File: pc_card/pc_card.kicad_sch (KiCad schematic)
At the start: 44 parts, among them IC1 SV 3.3V, IC2 74LVC1G00, IC3 SV 4.5V, IC4 TPA152DR, J1 PCMCIA Connector, J2 Headphones Out, U1 Z8601720ASG, U2 25LCxxx, U3 YMF289B-S, U4 YAC516-E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

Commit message: fixes
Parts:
- removed D1: D_Small_ALT, Diode_SMD:D_SOD-323_HandSoldering, symbol pc_card_sound_barker-rescue:D_Small_ALT-Device
- removed IC2: 74LVC1G00, Package_TO_SOT_SMD:SOT-23-5_HandSoldering, symbol pc_card_sound_barker-rescue:74LVC1G00-74xGxx
- removed JP3: Write Protect, Jumper:SolderJumper-3_P1.3mm_Bridged12_RoundedPad1.0x1.5mm_NumberLabels, symbol pc_card_sound_barker-rescue:SolderJumper_3_Bridged12-Jumper
- removed RN1: 20k, Resistor_SMD:R_Array_Convex_4x1206, symbol Device:R_Pack04_Split
- removed U2: 25LCxxx, Package_SO:SOIC-8_3.9x4.9mm_P1.27mm, symbol Memory_EEPROM:25LCxxx
- added R12: EEPROM, Resistor_SMD:R_0603_1608Metric_Pad0.98x0.95mm_HandSolder, symbol Device:R_Small
- added R3, R5, R6, R7: 20k, Resistor_SMD:R_0805_2012Metric_Pad1.20x1.40mm_HandSolder, symbol Device:R
- added U2: 93AAxxC, Package_SO:SOIC-8_3.9x4.9mm_P1.27mm, symbol Memory_EEPROM:93AAxxC
- IC4: footprint SOIC127P600X175-8N -> Package_SO:SOIC-8_3.9x4.9mm_P1.27mm
- U1: footprint QFP50P1600X1600X160-100N -> Package_QFP:LQFP-100_14x14mm_P0.5mm
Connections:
- net EE_CS: now also U2.1 (CS)
- net EE_DI: now also U2.4 (DO)
- net EE_DO: now also U2.3 (DI)
- net EE_SK: now also U2.2 (SCLK)
- net VCC: now also R12.1
- net VPP: now also R12.2, U2.8 (VCC)
- net at C13.1: now also R7.2
- net at IC4.8 (IN1-): now also R6.2, R7.1
- net at C10.2, IC4.1 (VO1), R4.2: now also R6.1
- net at IC4.4 (IN2-): now also R3.1, R5.2
- net at C14.2, IC4.5 (VO2), R8.1: now also R3.2
- net at C11.1: now also R5.1
- net GND renamed GNDA
- net GNDA: now also U2.5 (GND)
- no-connect marks 44 -> 45

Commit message: devboard; finishing 4L card
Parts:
- removed U2: 93AAxxC, Package_SO:SOIC-8_3.9x4.9mm_P1.27mm, symbol Memory_EEPROM:93AAxxC
- added R13: ORG, Resistor_SMD:R_0603_1608Metric_Pad0.98x0.95mm_HandSolder, symbol Device:R_Small
- added TP3: CS, TestPoint:TestPoint_Keystone_5015_Micro-Minature, symbol Connector:TestPoint_Probe
- added TP4: GND, TestPoint:TestPoint_Pad_D1.0mm, symbol Connector:TestPoint
- added TP5: RESET, TestPoint:TestPoint_Keystone_5015_Micro-Minature, symbol Connector:TestPoint_Probe
- added TP6: PWDN, TestPoint:TestPoint_Keystone_5015_Micro-Minature, symbol Connector:TestPoint_Probe
- added TP7: AUDIO, TestPoint:TestPoint_Keystone_5015_Micro-Minature, symbol Connector:TestPoint_Probe
- added TP8: 5V/~{3V}, TestPoint:TestPoint_Keystone_5015_Micro-Minature, symbol Connector:TestPoint_Probe
- added U2: 93CxxC, Package_SO:SOIC-8_3.9x4.9mm_P1.27mm, symbol Memory_EEPROM:93CxxC
- R10: footprint Resistor_SMD:R_0402_1005Metric_Pad0.72x0.64mm_HandSolder -> Resistor_SMD:R_0603_1608Metric_Pad0.98x0.95mm_HandSolder
- R11: footprint Resistor_SMD:R_1206_3216Metric_Pad1.30x1.75mm_HandSolder -> Resistor_SMD:R_0603_1608Metric_Pad0.98x0.95mm_HandSolder
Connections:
- net EE_CS: now also U2.1 (CS)
- net EE_DI: now also U2.4 (DO)
- net EE_DO: now also U2.3 (DI)
- net EE_SK: now also U2.2 (SCLK)
- net GNDA: now also R13.1, TP4.1, U2.5 (GND), U2.7 (TEST)
- net ICS0#: now also TP3.1
- net POR#: now also TP5.1
- net VPP: now also U2.8 (VCC)
- net at U1.59 (EXTP_PWDN): now also TP6.1
- net at U1.60 (EXTP_AUDIO): now also TP7.1
- net YMFVS renamed 5V/~{3V}
- net 5V/~{3V}: now also TP8.1
- new net: R13.2, U2.6 (ORG)
- no-connect marks 45 -> 42
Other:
- note removed: "Card Barker OPL3 Sound Card"
- note removed: "Nov 30 2021"
- note removed: "Prototype One"
- title: (none) -> Card Barker OPL3 Sound Card

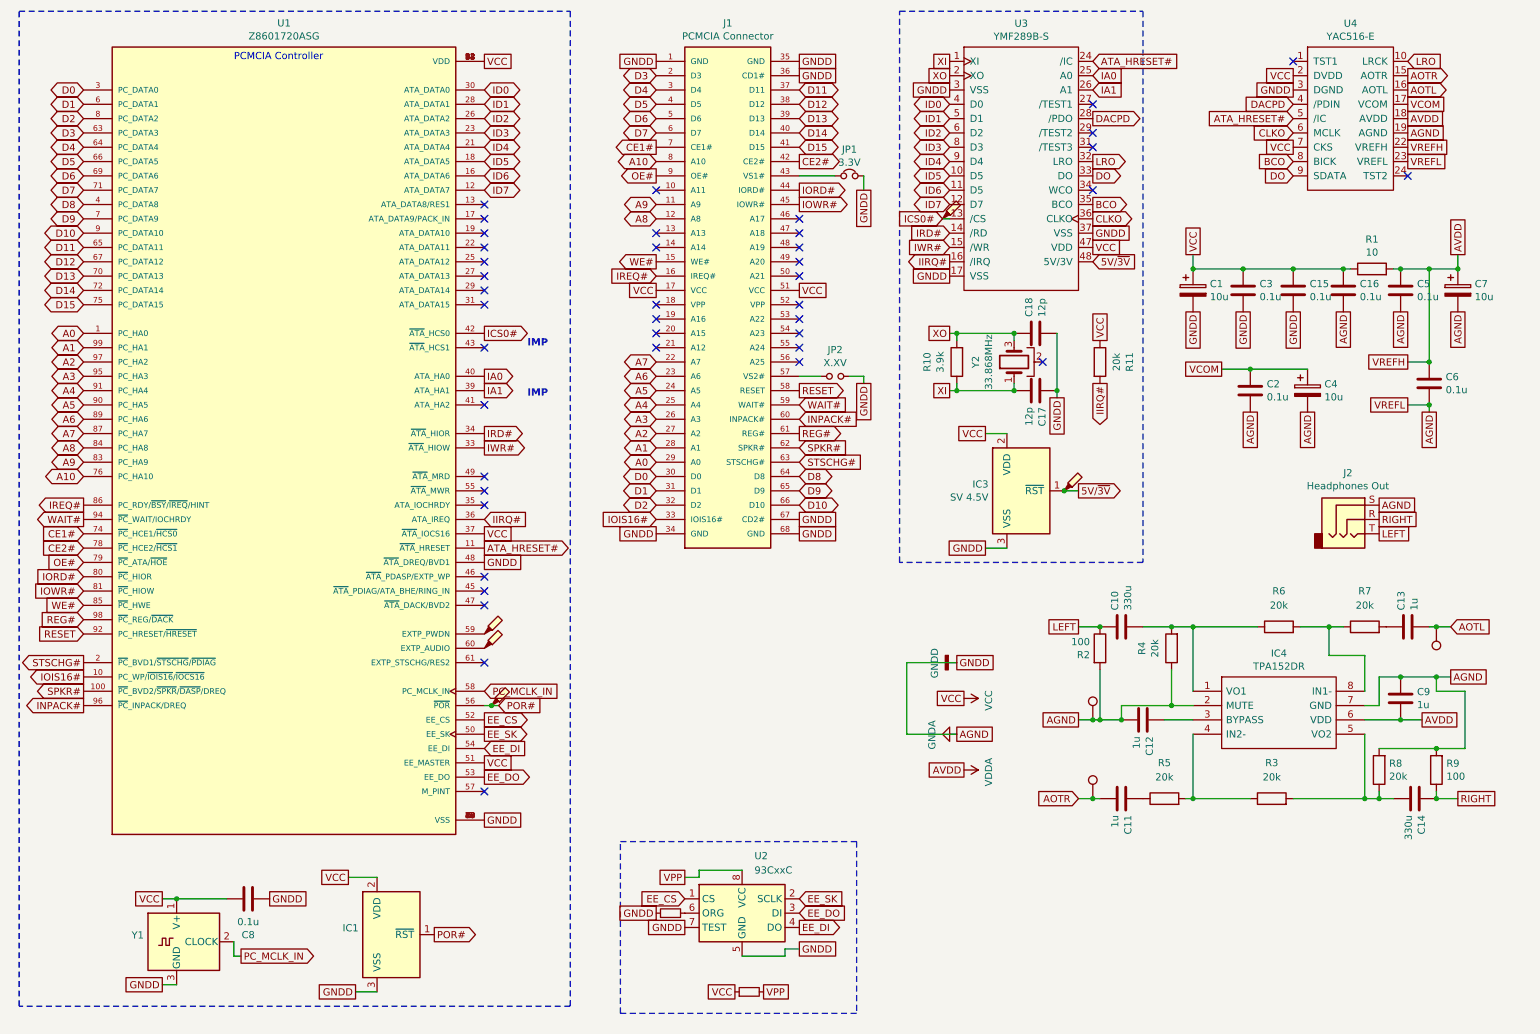
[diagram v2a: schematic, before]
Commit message: card hw rev 2 to manufacture
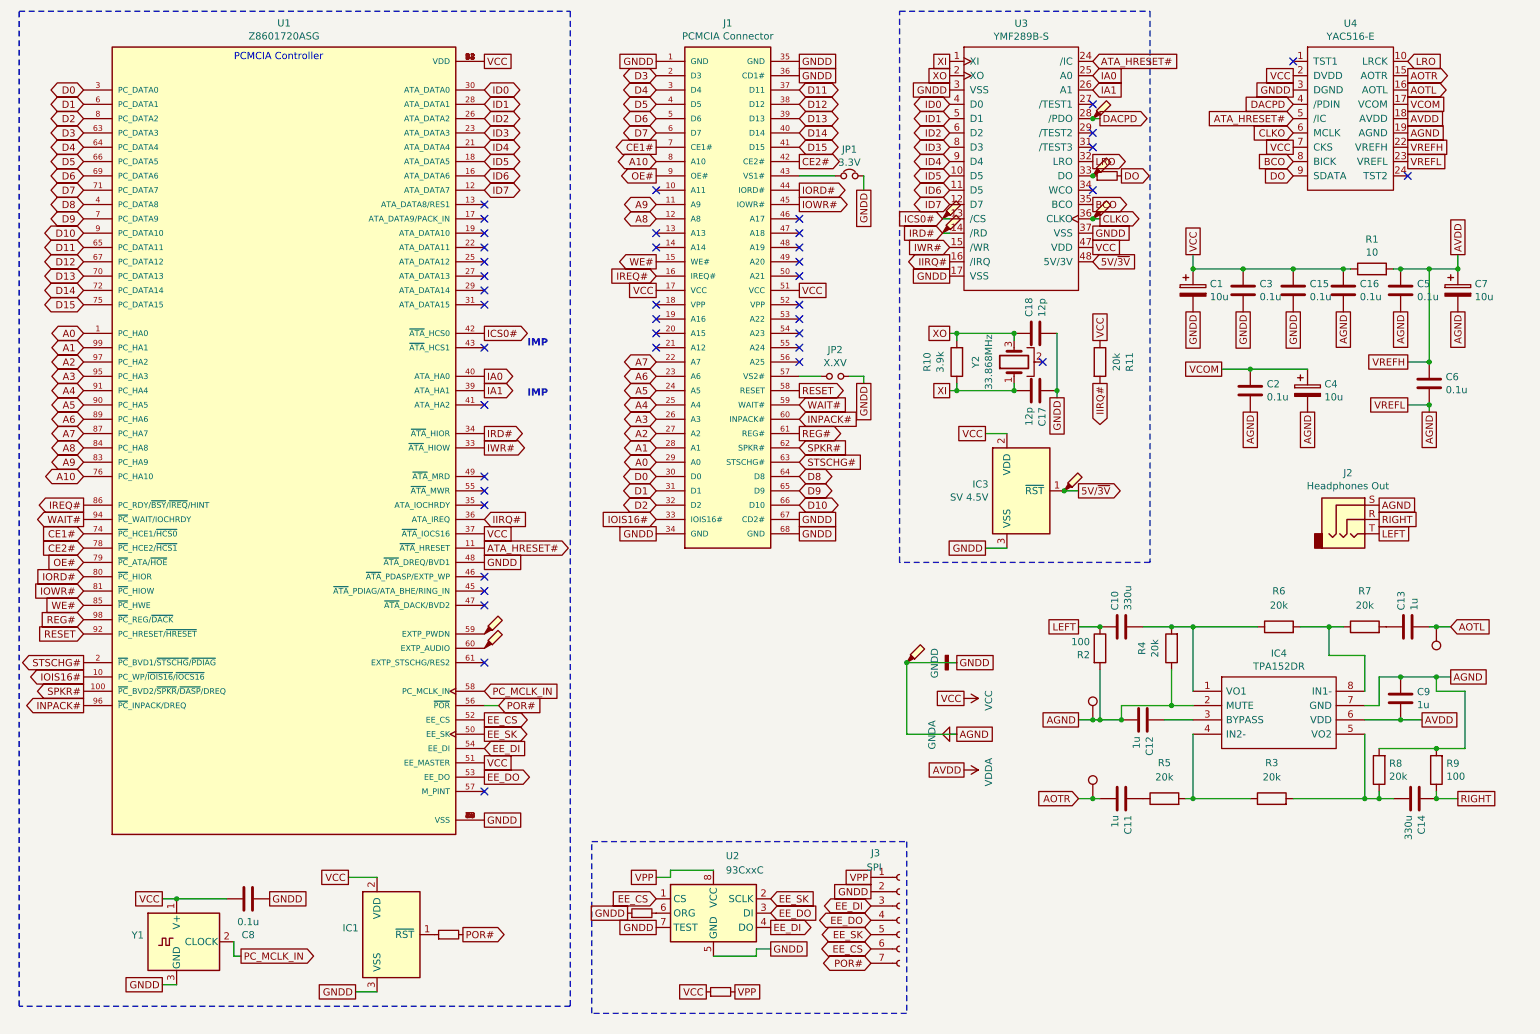
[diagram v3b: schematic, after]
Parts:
- added J3: SPI, Connector_PinHeader_1.27mm:PinHeader_1x07_P1.27mm_Vertical, symbol Connector:Conn_01x07_Socket
- added R14: DO, Resistor_SMD:R_0603_1608Metric_Pad0.98x0.95mm_HandSolder, symbol Device:R_Small
- added R15: ~{POR}, Resistor_SMD:R_0603_1608Metric_Pad0.98x0.95mm_HandSolder, symbol Device:R_Small
- added TP10: ~{RD}, TestPoint:TestPoint_Pad_1.0x1.0mm, symbol Connector:TestPoint_Probe
- added TP11: CK, TestPoint:TestPoint_Pad_1.0x1.0mm, symbol Connector:TestPoint_Probe
- added TP12: ~{PD}, TestPoint:TestPoint_Pad_1.0x1.0mm, symbol Connector:TestPoint_Probe
- added TP9: DO, TestPoint:TestPoint_Pad_1.0x1.0mm, symbol Connector:TestPoint_Probe
- TP3: value CS -> ~{CS}; footprint TestPoint:TestPoint_Keystone_5015_Micro-Minature -> TestPoint:TestPoint_Pad_1.0x1.0mm
- TP5: value RESET -> GND
- TP6, TP8: footprint TestPoint:TestPoint_Keystone_5015_Micro-Minature -> TestPoint:TestPoint_Pad_1.0x1.0mm
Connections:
- net CLKO: now also TP11.1
- net DACPD: now also TP12.1
- net DO: now also R14.2; no longer U3.33 (DO)
- net EE_CS: now also J3.6 (Pin_6)
- net EE_DI: now also J3.3 (Pin_3)
- net EE_DO: now also J3.4 (Pin_4)
- net EE_SK: now also J3.5 (Pin_5)
- net GNDA: now also TP5.1, J3.2 (Pin_2)
- net IRD#: now also TP10.1
- net POR#: now also J3.7 (Pin_7), R15.2; no longer IC1.1 (~{RST}), TP5.1
- net VPP: now also J3.1 (Pin_1)
- new net: R14.1, TP9.1, U3.33 (DO)
- new net: IC1.1 (~{RST}), R15.1
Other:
- moved on the sheet: U2

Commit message: hw rev3
* reDfMing the card so the connector can be assembled easier
* added software and specs
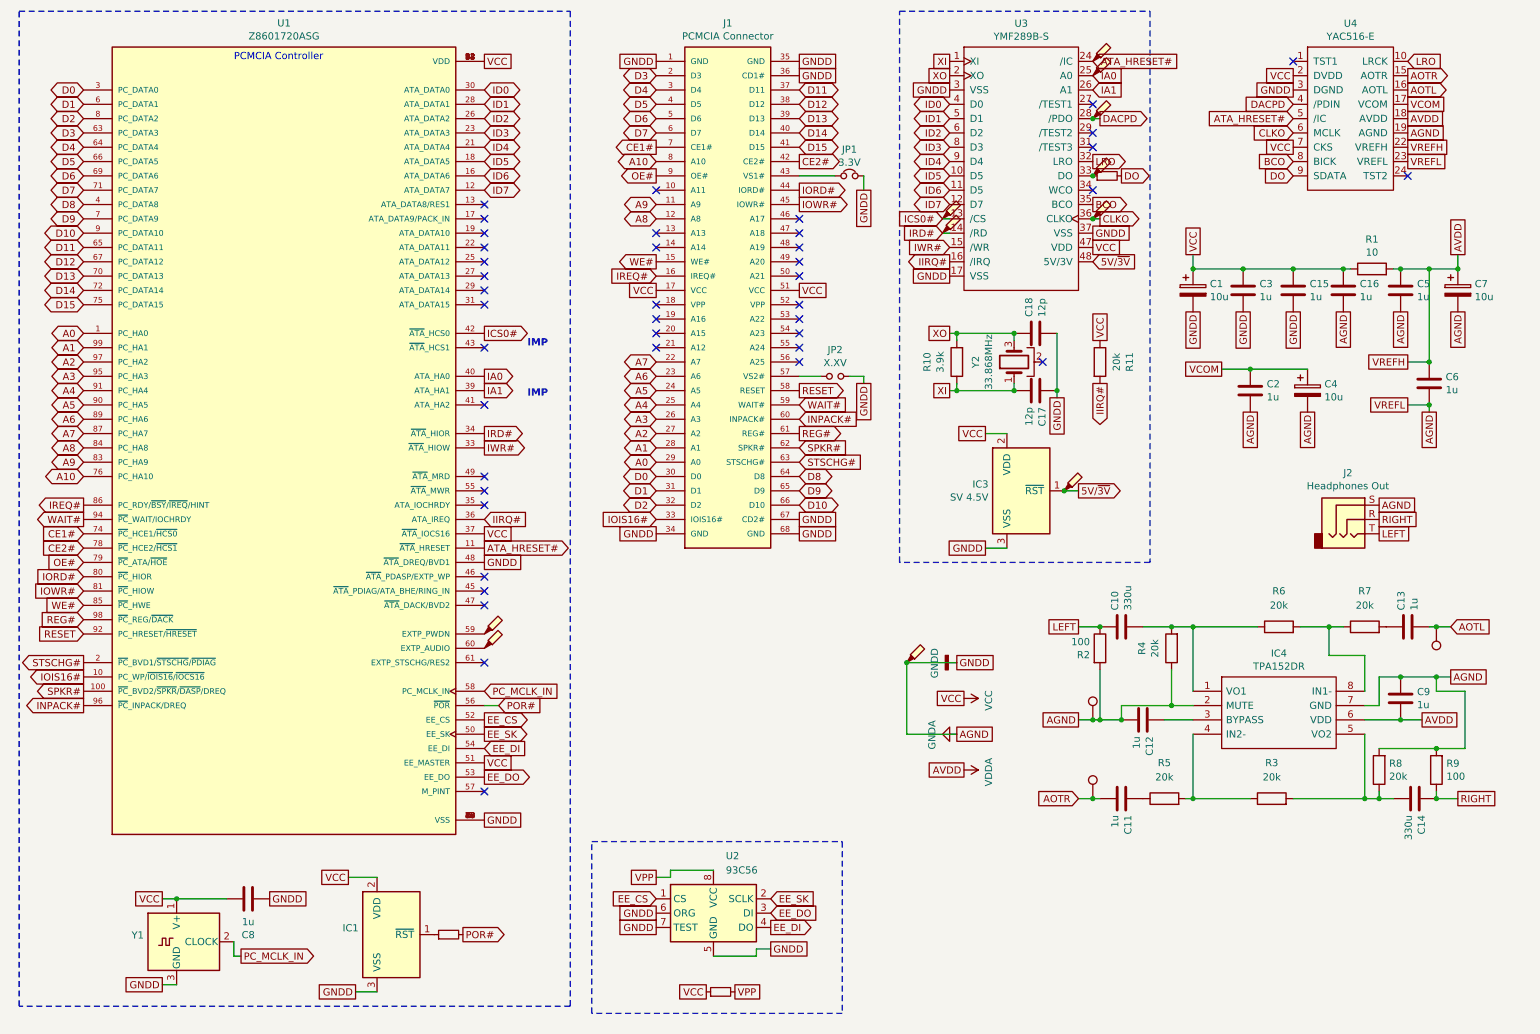
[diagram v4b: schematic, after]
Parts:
- removed J3: SPI, Connector_PinHeader_1.27mm:PinHeader_1x07_P1.27mm_Vertical, symbol Connector:Conn_01x07_Socket
- removed R13: ORG, Resistor_SMD:R_0603_1608Metric_Pad0.98x0.95mm_HandSolder, symbol Device:R_Small
- added TP13: A0, TestPoint:TestPoint_Pad_1.0x1.0mm, symbol Connector:TestPoint_Probe
- added TP14: ~{RESET}, TestPoint:TestPoint_Pad_1.0x1.0mm, symbol Connector:TestPoint_Probe
- C15, C16, C2, C3, C5, C6, C8: value 0.1u -> 1u
- IC3: Manufacturer_Name Texas Instruments -> Microchip Technology; Manufacturer_Part_Number TLV809EA45DBZR -> MCP102T-450E/TT; Mouser Part Number 595-TLV809EA45DBZR -> (none); Mouser Price/Stock https://www.mouser.co.uk/ProductDetail/595-TLV809EA45DBZR -> (none)
- TP7: footprint TestPoint:TestPoint_Keystone_5015_Micro-Minature -> TestPoint:TestPoint_Pad_1.0x1.0mm
- U2: value 93CxxC -> 93C56
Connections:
- net ATA_HRESET#: now also TP14.1
- net GNDA: now also U2.6 (ORG)
- net IA0: now also TP13.1

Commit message: fiddling with connector
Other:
- title: Card Barker OPL3 Sound Card -> PCMCIA OPL3 Sound Card
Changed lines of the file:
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@@
 	(paper "A4")
 	(title_block
-		(title "Card Barker OPL3 Sound Card")
-		(date "2024-08-07")
-		(rev "HW2")
+		(title "PCMCIA OPL3 Sound Card")
+		(date "2025-02-06")
+		(rev "HW3")
 	)
 	(junction
